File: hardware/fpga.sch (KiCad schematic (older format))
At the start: 73 parts, among them J1 SD_Card, P3 CONN_02X04, P4 CONN_02X04, Q2 DNP(RE1C002UN), SW2 SW_PUSH, U30 XC7A15T-FTG256, U40 W25Q32JV

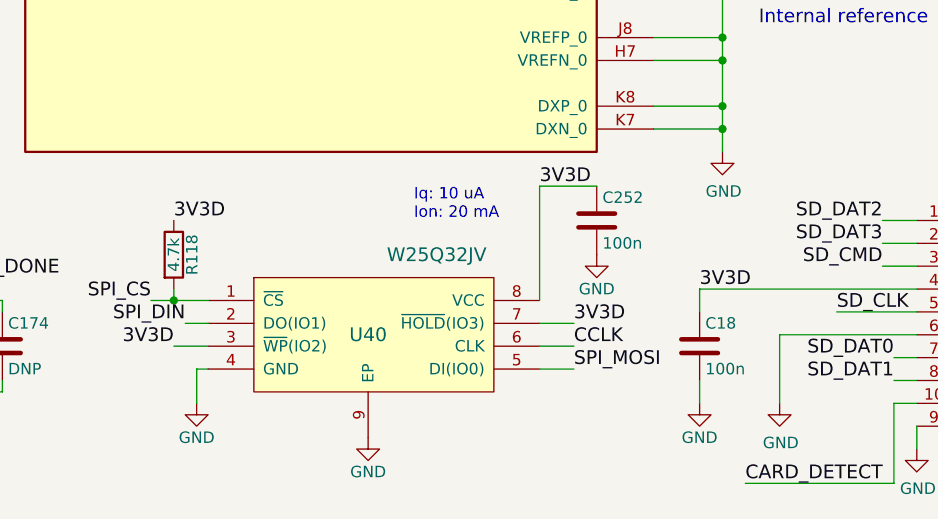
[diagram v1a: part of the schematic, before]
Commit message: Improved documentation and parts of the schematic.
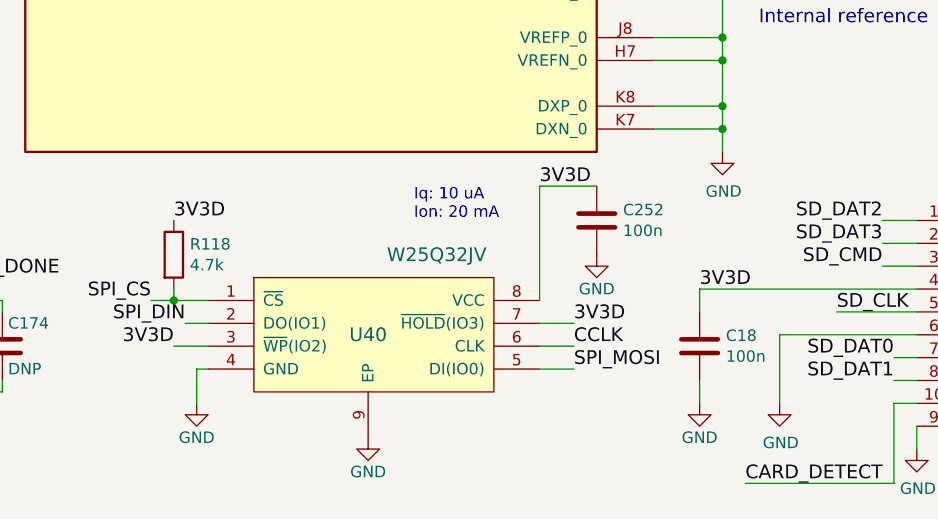
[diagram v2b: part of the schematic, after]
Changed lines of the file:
@@
 U 1 1 5856F6DD
 P 7750 10000
-F 0 "C252" H 7775 10100 50  0000 L CNN
-F 1 "100n" H 7775 9900 50  0000 L CNN
+F 0 "C252" H 7865 10046 50  0000 L CNN
+F 1 "100n" H 7865 9955 50  0000 L CNN
 F 2 "Capacitor_SMD:C_0402_1005Metric" H 7788 9850 30  0001 C CNN
 F 3 "" H 7750 10000 60  0000 C CNN
@@
 U 1 1 5857A8B8
 P 5900 10150
-F 0 "R118" V 5980 10150 50  0000 C CNN
-F 1 "4.7k" V 5900 10150 50  0000 C CNN
+F 0 "R118" H 5970 10196 50  0000 L CNN
+F 1 "4.7k" H 5970 10105 50  0000 L CNN
 F 2 "Resistor_SMD:R_0402_1005Metric" V 5830 10150 30  0001 C CNN
 F 3 "" H 5900 10150 30  0000 C CNN
@@
 U 1 1 595AE318
 P 8200 10550
-F 0 "C18" H 8225 10650 50  0000 L CNN
-F 1 "100n" H 8225 10450 50  0000 L CNN
+F 0 "C18" H 8315 10596 50  0000 L CNN
+F 1 "100n" H 8315 10505 50  0000 L CNN
 F 2 "Capacitor_SMD:C_0402_1005Metric" H 8238 10400 30  0001 C CNN
 F 3 "" H 8200 10550 60  0000 C CNN

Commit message: Changed components to official libs.
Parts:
- SW2: symbol fmcw-rescue:SW_PUSH-fmcw3-rescue -> Switch:SW_Push
- U40: footprint Package_DFN_QFN:DFN-S-8-1EP_6x5mm_P1.27mm -> Package_DFN_QFN:DFN-8-1EP_6x5mm_P1.27mm_EP3.4x4.3mm; symbol fmcw-rescue:W25Q32JV-fmcw3-rescue -> Memory_Flash:W25Q32JVZP
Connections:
- net 3V3D: now also C252.2; no longer C252.1
- net GND: now also C252.1; no longer C252.2
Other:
- moved on the sheet: C171, C252, P4, R118, SW2, U40

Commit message: Finished design, began routing.
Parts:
- C20: renamed from C226; footprint Capacitor_SMD:C_1210_3225Metric -> Capacitor_SMD:C_1206_3216Metric
- renumbered C205 to C14, C170 to C15, C171 to C16, C174 to C17, C252 to C18, C18 to C19, C235 to C21, C182 to C22, C236 to C23, C237 to C24, C185 to C25, C238 to C26, C188 to C27, C239 to C28, C240 to C29, C190 to C30, C194 to C31, C195 to C32, C192 to C33, C197 to C34, C193 to C35, C198 to C36, C199 to C37, C181 to C38, C200 to C39, C201 to C40, C183 to C41, C202 to C42, C203 to C43, C186 to C44, C204 to C45, C251 to C46, C189 to C47, C241 to C48, C191 to C49, C242 to C50, C243 to C51, C184 to C52, C244 to C53, C187 to C54, C245 to C55, C246 to C56, C247 to C57, C196 to C58, D6 to D1, P4 to P1, P3 to P2, Q2 to Q1, R117 to R10, R118 to R11, R111 to R12, R115 to R13, R130 to R14, R114 to R15, R110 to R16, R109 to R6, R69 to R7, R70 to R8, R112 to R9, SW2 to SW1, U30 to U6, U40 to U7
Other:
- moved on the sheet: C15, C16, D1, P1, P2, R6, R7

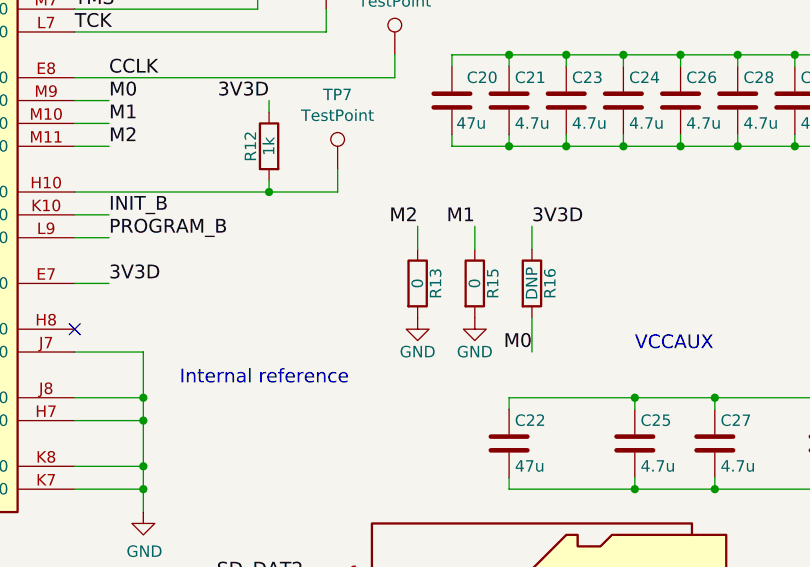
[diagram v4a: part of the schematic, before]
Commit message: Completed clock placement and routing.
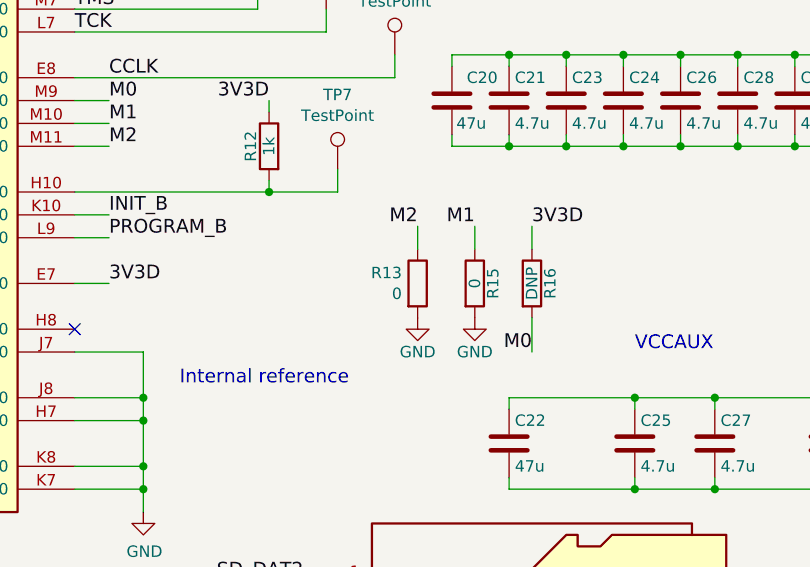
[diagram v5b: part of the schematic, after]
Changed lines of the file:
@@
 U 1 1 58553EF2
 P 9500 8700
-F 0 "R13" V 9580 8700 50  0000 C CNN
-F 1 "0" V 9500 8700 50  0000 C CNN
+F 0 "R13" H 9431 8746 50  0000 R CNN
+F 1 "0" H 9431 8655 50  0000 R CNN
 F 2 "Resistor_SMD:R_0402_1005Metric" V 9430 8700 30  0001 C CNN
 F 3 "" H 9500 8700 30  0000 C CNN
 F 4 "ERJ-2GE0R00X" H 0   0   50  0001 C CNN "MFN"
 	1    9500 8700
-	1    0    0    -1
-$EndComp
-$Comp
-L Device:R R15
-U 1 1 58553D4B
-P 9750 8700
-F 0 "R15" V 9830 8700 50  0000 C CNN
-F 1 "0" V 9750 8700 50  0000 C CNN
-F 2 "Resistor_SMD:R_0402_1005Metric" V 9680 8700 30  0001 C CNN
-F 3 "" H 9750 8700 30  0000 C CNN
-F 4 "ERJ-2GE0R00X" H 0   0   50  0001 C CNN "MFN"
-	1    9750 8700
 	1    0    0    -1
 $EndComp
@@
 	1    0    0    -1
 $EndComp
+$Comp
+L Device:R R15
+U 1 1 58553D4B
+P 9750 8700
+F 0 "R15" V 9830 8700 50  0000 C CNN
+F 1 "0" V 9750 8700 50  0000 C CNN
+F 2 "Resistor_SMD:R_0402_1005Metric" V 9680 8700 30  0001 C CNN
+F 3 "" H 9750 8700 30  0000 C CNN
+F 4 "ERJ-2GE0R00X" H 0   0   50  0001 C CNN "MFN"
+	1    9750 8700
+	1    0    0    -1
+$EndComp

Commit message: Improved silkscreen appearance.
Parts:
- C14, C15, C16, C30, C33, C34, C35, C36, C37, C39, C40, C42, C43, C45, C46, C47, C48, C49, C50, C51, C53, C54, C55, C56, C57: MFN GRM188R70J474KA01 -> GRM188R70J474KA01D
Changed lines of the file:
@@
 F 2 "Capacitor_SMD:C_0603_1608Metric" H 15688 7750 30  0001 C CNN
 F 3 "" H 15650 7900 60  0000 C CNN
-F 4 "GRM188R70J474KA01" H 0   0   50  0001 C CNN "MFN"
+F 4 "GRM188R70J474KA01D" H 0   0   50  0001 C CNN "MFN"
 	1    15650 7900
 	1    0    0    -1
@@
 F 2 "Capacitor_SMD:C_0603_1608Metric" H 15438 7750 30  0001 C CNN
 F 3 "" H 15400 7900 60  0000 C CNN
-F 4 "GRM188R70J474KA01" H 0   0   50  0001 C CNN "MFN"
+F 4 "GRM188R70J474KA01D" H 0   0   50  0001 C CNN "MFN"
 	1    15400 7900
 	1    0    0    -1
@@
 F 2 "Capacitor_SMD:C_0603_1608Metric" H 15188 7750 30  0001 C CNN
 F 3 "" H 15150 7900 60  0000 C CNN
-F 4 "GRM188R70J474KA01" H 0   0   50  0001 C CNN "MFN"
+F 4 "GRM188R70J474KA01D" H 0   0   50  0001 C CNN "MFN"
 	1    15150 7900
 	1    0    0    -1
@@
 F 2 "Capacitor_SMD:C_0603_1608Metric" H 14938 7750 30  0001 C CNN
 F 3 "" H 14900 7900 60  0000 C CNN
-F 4 "GRM188R70J474KA01" H 0   0   50  0001 C CNN "MFN"
+F 4 "GRM188R70J474KA01D" H 0   0   50  0001 C CNN "MFN"
 	1    14900 7900
 	1    0    0    -1
@@
 F 2 "Capacitor_SMD:C_0603_1608Metric" H 14688 7750 30  0001 C CNN
 F 3 "" H 14650 7900 60  0000 C CNN
-F 4 "GRM188R70J474KA01" H 0   0   50  0001 C CNN "MFN"
+F 4 "GRM188R70J474KA01D" H 0   0   50  0001 C CNN "MFN"
 	1    14650 7900
 	1    0    0    -1
@@
 F 2 "Capacitor_SMD:C_0603_1608Metric" H 14438 7750 30  0001 C CNN
 F 3 "" H 14400 7900 60  0000 C CNN
-F 4 "GRM188R70J474KA01" H 0   0   50  0001 C CNN "MFN"
+F 4 "GRM188R70J474KA01D" H 0   0   50  0001 C CNN "MFN"
 	1    14400 7900
 	1    0    0    -1
@@
 F 2 "Capacitor_SMD:C_0603_1608Metric" H 14188 7750 30  0001 C CNN
 F 3 "" H 14150 7900 60  0000 C CNN
-F 4 "GRM188R70J474KA01" H 0   0   50  0001 C CNN "MFN"
+F 4 "GRM188R70J474KA01D" H 0   0   50  0001 C CNN "MFN"
 	1    14150 7900
 	1    0    0    -1
@@
 F 2 "Capacitor_SMD:C_0603_1608Metric" H 2438 9800 30  0001 C CNN
 F 3 "" H 2400 9950 60  0000 C CNN
-F 4 "GRM188R70J474KA01" H 250 -100 50  0001 C CNN "MFN"
+F 4 "GRM188R70J474KA01D" H 250 -100 50  0001 C CNN "MFN"
 	1    2400 9950
 	1    0    0    -1
@@
 F 2 "Capacitor_SMD:C_0603_1608Metric" H 2388 10550 30  0001 C CNN
 F 3 "" H 2350 10700 60  0000 C CNN
-F 4 "GRM188R70J474KA01" H 250 0   50  0001 C CNN "MFN"
+F 4 "GRM188R70J474KA01D" H 250 0   50  0001 C CNN "MFN"
 	1    2350 10700
 	1    0    0    -1
@@
 F 2 "Capacitor_SMD:C_0603_1608Metric" H 13938 7750 30  0001 C CNN
 F 3 "" H 13900 7900 60  0000 C CNN
-F 4 "GRM188R70J474KA01" H 0   0   50  0001 C CNN "MFN"
+F 4 "GRM188R70J474KA01D" H 0   0   50  0001 C CNN "MFN"
 	1    13900 7900
 	1    0    0    -1
@@
 F 2 "Capacitor_SMD:C_0603_1608Metric" H 1038 6850 30  0001 C CNN
 F 3 "" H 1000 7000 60  0000 C CNN
-F 4 "GRM188R70J474KA01" H 0   0   50  0001 C CNN "MFN"
+F 4 "GRM188R70J474KA01D" H 0   0   50  0001 C CNN "MFN"
 	1    1000 7000
 	1    0    0    -1
@@
 F 2 "Capacitor_SMD:C_0603_1608Metric" H 11938 7750 30  0001 C CNN
 F 3 "" H 11900 7900 60  0000 C CNN
-F 4 "GRM188R70J474KA01" H 0   0   50  0001 C CNN "MFN"
+F 4 "GRM188R70J474KA01D" H 0   0   50  0001 C CNN "MFN"
 	1    11900 7900
 	1    0    0    -1
@@
 F 2 "Capacitor_SMD:C_0603_1608Metric" H 12188 7750 30  0001 C CNN
 F 3 "" H 12150 7900 60  0000 C CNN
-F 4 "GRM188R70J474KA01" H 0   0   50  0001 C CNN "MFN"
+F 4 "GRM188R70J474KA01D" H 0   0   50  0001 C CNN "MFN"
 	1    12150 7900
 	1    0    0    -1
@@
 F 2 "Capacitor_SMD:C_0603_1608Metric" H 12438 7750 30  0001 C CNN
 F 3 "" H 12400 7900 60  0000 C CNN
-F 4 "GRM188R70J474KA01" H 0   0   50  0001 C CNN "MFN"
+F 4 "GRM188R70J474KA01D" H 0   0   50  0001 C CNN "MFN"
 	1    12400 7900
 	1    0    0    -1
@@
 F 2 "Capacitor_SMD:C_0603_1608Metric" H 12688 7750 30  0001 C CNN
 F 3 "" H 12650 7900 60  0000 C CNN
-F 4 "GRM188R70J474KA01" H 0   0   50  0001 C CNN "MFN"
+F 4 "GRM188R70J474KA01D" H 0   0   50  0001 C CNN "MFN"
 	1    12650 7900
 	1    0    0    -1
@@
 F 2 "Capacitor_SMD:C_0603_1608Metric" H 12938 7750 30  0001 C CNN
 F 3 "" H 12900 7900 60  0000 C CNN
-F 4 "GRM188R70J474KA01" H 0   0   50  0001 C CNN "MFN"
+F 4 "GRM188R70J474KA01D" H 0   0   50  0001 C CNN "MFN"
 	1    12900 7900
 	1    0    0    -1
@@
 F 2 "Capacitor_SMD:C_0603_1608Metric" H 13188 7750 30  0001 C CNN
 F 3 "" H 13150 7900 60  0000 C CNN
-F 4 "GRM188R70J474KA01" H 0   0   50  0001 C CNN "MFN"
+F 4 "GRM188R70J474KA01D" H 0   0   50  0001 C CNN "MFN"
 	1    13150 7900
 	1    0    0    -1
@@
 F 2 "Capacitor_SMD:C_0603_1608Metric" H 11688 9250 30  0001 C CNN
 F 3 "" H 11650 9400 60  0000 C CNN
-F 4 "GRM188R70J474KA01" H 0   0   50  0001 C CNN "MFN"
+F 4 "GRM188R70J474KA01D" H 0   0   50  0001 C CNN "MFN"
 	1    11650 9400
 	1    0    0    -1
@@
 F 2 "Capacitor_SMD:C_0603_1608Metric" H 11338 9250 30  0001 C CNN
 F 3 "" H 11300 9400 60  0000 C CNN
-F 4 "GRM188R70J474KA01" H 0   0   50  0001 C CNN "MFN"
+F 4 "GRM188R70J474KA01D" H 0   0   50  0001 C CNN "MFN"
 	1    11300 9400
 	1    0    0    -1
@@
 F 2 "Capacitor_SMD:C_0603_1608Metric" H 15138 8650 30  0001 C CNN
 F 3 "" H 15100 8800 60  0000 C CNN
-F 4 "GRM188R70J474KA01" H 0   0   50  0001 C CNN "MFN"
+F 4 "GRM188R70J474KA01D" H 0   0   50  0001 C CNN "MFN"
 	1    15100 8800
 	1    0    0    -1
@@
 F 2 "Capacitor_SMD:C_0603_1608Metric" H 13438 7750 30  0001 C CNN
 F 3 "" H 13400 7900 60  0000 C CNN
-F 4 "GRM188R70J474KA01" H 0   0   50  0001 C CNN "MFN"
+F 4 "GRM188R70J474KA01D" H 0   0   50  0001 C CNN "MFN"
 	1    13400 7900
 	1    0    0    -1
@@
 F 2 "Capacitor_SMD:C_0603_1608Metric" H 13688 7750 30  0001 C CNN
 F 3 "" H 13650 7900 60  0000 C CNN
-F 4 "GRM188R70J474KA01" H 0   0   50  0001 C CNN "MFN"
+F 4 "GRM188R70J474KA01D" H 0   0   50  0001 C CNN "MFN"
 	1    13650 7900
 	1    0    0    -1
@@
 F 2 "Capacitor_SMD:C_0603_1608Metric" H 14288 9300 30  0001 C CNN
 F 3 "" H 14250 9450 60  0000 C CNN
-F 4 "GRM188R70J474KA01" H 0   0   50  0001 C CNN "MFN"
+F 4 "GRM188R70J474KA01D" H 0   0   50  0001 C CNN "MFN"
 	1    14250 9450
 	1    0    0    -1
@@
 F 2 "Capacitor_SMD:C_0603_1608Metric" H 13938 9300 30  0001 C CNN
 F 3 "" H 13900 9450 60  0000 C CNN
-F 4 "GRM188R70J474KA01" H 0   0   50  0001 C CNN "MFN"
+F 4 "GRM188R70J474KA01D" H 0   0   50  0001 C CNN "MFN"
 	1    13900 9450
 	1    0    0    -1
@@
 F 2 "Capacitor_SMD:C_0603_1608Metric" H 12038 9250 30  0001 C CNN
 F 3 "" H 12000 9400 60  0000 C CNN
-F 4 "GRM188R70J474KA01" H 0   0   50  0001 C CNN "MFN"
+F 4 "GRM188R70J474KA01D" H 0   0   50  0001 C CNN "MFN"
 	1    12000 9400
 	1    0    0    -1
